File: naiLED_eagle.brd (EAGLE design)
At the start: 12.4 x 12.7 mm, 8 parts, among them IC1 TCS3414, U2 24LC00T-I/OT, U3 ATTINY25-20SSU

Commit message: Update naiLED_eagle.brd
board layout design by florin lazar
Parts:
- added E$1: (no value), Logo:OSHW_FILLX100_NOTEXT
- moved R6 0.84 mm to (1.70, 7.16)
- moved R5 0.81 mm to (6.43, 7.29), turned to 270 degrees
- moved C1 0.76 mm to (1.70, 4.55)
- moved IC1 0.20 mm to (9.17, 7.59)
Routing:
- net VCC: track 0.00 -> 37.9 mm, vias 0 -> 3
- net D0/PWM/MOSI/SDA: track 1.52 -> 26.0 mm, vias 0 -> 4
- net D2/A1/SCK/SCL: track 0.00 -> 23.1 mm, vias 0 -> 4
- net D1/PWM/MISO: track 0.00 -> 21.5 mm, vias 0 -> 1
- net D4/PWM: track 0.00 -> 18.7 mm
- net D3/A3: track 0.00 -> 15.2 mm
- net D5/A0/RESET: track 0.00 -> 14.8 mm, vias 0 -> 3
- net GND: vias 0 -> 5
- added copper zone on layer 1, net GND
- added copper zone on layer 16, net GND
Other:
- board text added: "yair.cc/nld"
- board text removed: "EEPROM"

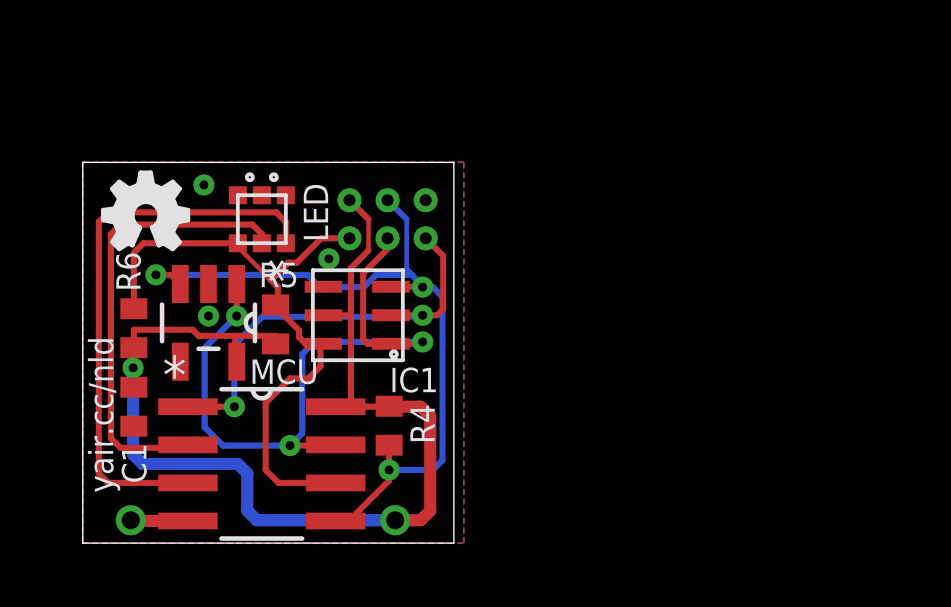
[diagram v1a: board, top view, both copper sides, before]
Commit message: added library
ripup all , changed LED to CLPP4 and added resistors
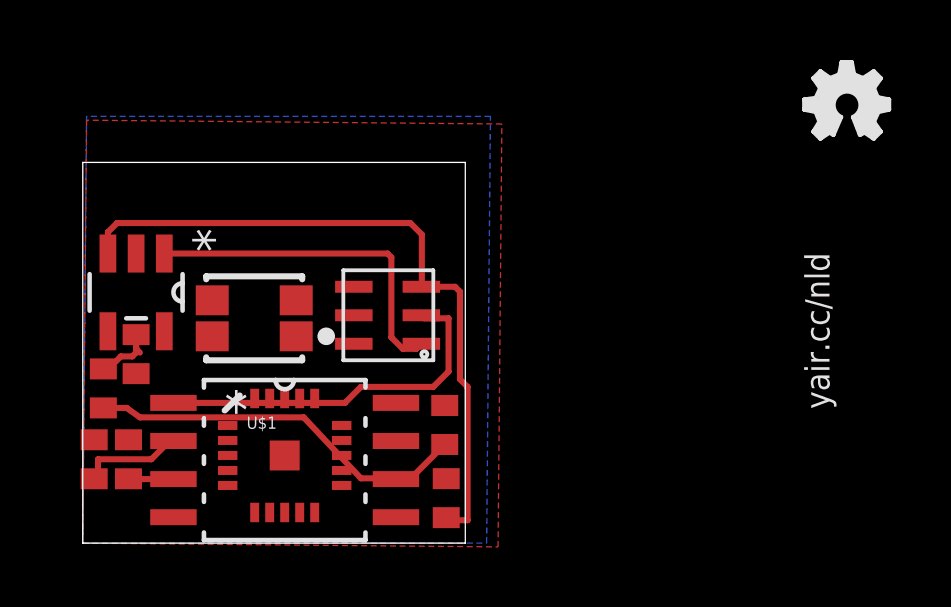
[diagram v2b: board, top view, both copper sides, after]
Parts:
- removed LED1: LED_RGB3, dp_devices:RGBLED
- removed R6: (no value), dp_devices:R402
- added LED2: (no value), microbuilder:RGBLED_PLCC4
- added R1, R2, R3: (no value), dp_devices:R402
- added U$1: ATTINY24QFN, SparkFun-DigitalIC:QFN20
- U3: value ATTINY25-20SSU -> ATTINY85-20SU; device yair_r:SOIC127P600X175-8N -> nld:SOIC127P798X216-8N
- moved E$1 23.7 mm to (24.1, 13.5)
- moved R5 6.12 mm to (0.69, 5.16), turned to 90 degrees
- moved R4 3.07 mm to (12.1, 1.50)
- moved U2 2.62 mm to (1.78, 8.36)
- moved C1 1.75 mm to (1.78, 6.30)
- moved IC1 1.02 mm to (10.2, 7.59)
- moved U3 0.77 mm to (6.73, 2.77)
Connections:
- new net N$1: LED2.1, R3.1
- new net N$2: LED2.4, R2.1
- new net N$3: LED2.3, R1.1
- net D1/PWM/MISO: now also R3.2; no longer IC1.P$4, LED1.AG, R6.2
- net D3/A3: now also R2.2; no longer LED1.AR
- net D4/PWM: now also R1.2; no longer LED1.AB
- net GND: no longer LED1.CB, LED1.CG, LED1.CR
- net VCC: now also LED2.2; no longer R6.1
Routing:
- net VCC: track 37.9 -> 2.57 mm, vias 3 -> 0
- net D4/PWM: track 18.7 -> 1.51 mm
- net D3/A3: track 15.2 -> 3.47 mm
- net D2/A1/SCK/SCL: track 23.1 -> 11.5 mm, vias 4 -> 0
- net D1/PWM/MISO: track 21.5 -> 12.8 mm, vias 1 -> 0
- net D0/PWM/MOSI/SDA: track 26.0 -> 23.0 mm, vias 4 -> 0
- net D5/A0/RESET: track 14.8 -> 12.3 mm, vias 3 -> 0
- net GND: track 1.50 -> 0.00 mm, vias 5 -> 0
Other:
- board size 12.4 x 12.7 mm -> 12.8 x 12.7 mm
- board text removed: "LED"
- board text removed: "MCU"

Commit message: working on the at841
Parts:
- removed U$1: ATTINY24QFN, SparkFun-DigitalIC:QFN20
- removed U3: ATTINY85-20SU, nld:SOIC127P798X216-8N
- added GND-TAB, VCC-TAB: (no value), adafruit:1X01-CLEANBIG
- added IC2: ATTINY441/841-MU, nld:20MLF_0.5
- moved R4 9.81 mm to (2.69, 4.24), turned to 180 degrees
- moved R1 9.22 mm to (9.53, 7.37)
- moved R2 9.22 mm to (8.38, 7.37)
- moved R3 7.99 mm to (4.45, 6.35)
- moved C1 5.30 mm to (3.30, 1.22)
- moved R5 2.98 mm to (2.72, 2.97), turned to 180 degrees
- moved IC1 2.85 mm to (10.1, 10.4), turned to 0 degrees
- moved LED2 2.16 mm to (5.71, 9.65), turned to 90 degrees
- moved U2 1.40 mm to (1.91, 6.96)
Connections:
- removed net D0/PWM/MOSI/SDA: IC1.P$3, R4.1, U2.3, U3.5
- removed net D1/PWM/MISO: R3.2, R5.1, U3.6
- removed net D2/A1/SCK/SCL: IC1.P$1, U2.1, U3.7
- removed net D3/A3: R2.2, U3.2
- removed net D4/PWM: R1.2, U3.3
- new net MISO: IC2.5, R5.1
- new net MOSI: IC1.P$3, IC2.4, R4.1, U2.3
- new net N$4: IC2.15, R1.2
- new net N$5: IC2.16, R2.2
- new net N$6: IC2.20, R3.2
- new net SCL: IC1.P$1, IC2.1, U2.1
- net D5/A0/RESET: no longer U3.1
- net GND: now also GND-TAB.1, IC2.8; no longer U3.4
- net VCC: now also IC2.9, VCC-TAB.1; no longer U3.8
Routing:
- net D0/PWM/MOSI/SDA: track 23.0 -> 0.00 mm
- net SCL: track 0.00 -> 13.6 mm
- net D1/PWM/MISO: track 12.8 -> 0.00 mm
- net D5/A0/RESET: track 12.3 -> 0.00 mm
- net D2/A1/SCK/SCL: track 11.5 -> 0.00 mm
- net GND: track 0.00 -> 10.1 mm, vias 0 -> 2
- net MOSI: track 0.00 -> 7.06 mm
- net N$3: track 0.00 -> 4.71 mm
- net N$2: track 0.00 -> 4.46 mm
- net D3/A3: track 3.47 -> 0.00 mm
- net VCC: track 2.57 -> 0.00 mm
- net N$4: track 0.00 -> 2.30 mm
- net MISO: track 0.00 -> 1.53 mm
- net D4/PWM: track 1.51 -> 0.00 mm
- net N$1: track 0.00 -> 1.42 mm
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- added copper zone on layer 1, net VCC
- removed copper zone on layer 1, net GND

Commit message: some changes, not major
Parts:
- moved U2 9.12 mm to (10.8, 4.83), turned to 180 degrees
- moved IC1 8.16 mm to (2.44, 7.72), turned to 180 degrees
- moved C1 5.99 mm to (9.27, 1.73)
- moved R3 5.10 mm to (9.27, 8.00)
- moved R1 2.37 mm to (11.8, 8.00)
- moved R2 2.25 mm to (10.5, 8.00)
- moved LED2 1.31 mm to (6.35, 8.51)
- moved R4 1.02 mm to (1.68, 4.37)
- moved R5 1.02 mm to (1.70, 2.97)
- moved IC2 0.89 mm to (3.94, 1.52)
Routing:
- net SCL: track 13.6 -> 0.00 mm
- net GND: track 10.1 -> 0.00 mm, vias 2 -> 0
- net MOSI: track 7.06 -> 0.00 mm
- net N$3: track 4.71 -> 0.00 mm
- net N$2: track 4.46 -> 0.00 mm
- net N$4: track 2.30 -> 0.00 mm
- net MISO: track 1.53 -> 0.00 mm
- net N$1: track 1.42 -> 0.00 mm
- net N$6: track 1.39 -> 0.00 mm
- net N$5: track 1.32 -> 0.00 mm
- added copper zone on layer 1, net GND
- removed copper zone on layer 1, net VCC
